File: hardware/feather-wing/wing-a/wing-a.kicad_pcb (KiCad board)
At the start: 2 copper layers, 50.8 x 22.9 mm, 29 parts, among them J1 USB-C plug, J2 Feather 16-pin, J3 Feather 12-pin, U2 AP22653W6-7, U3 USBLC6-2SC6, U4 USBLC6-2SC6

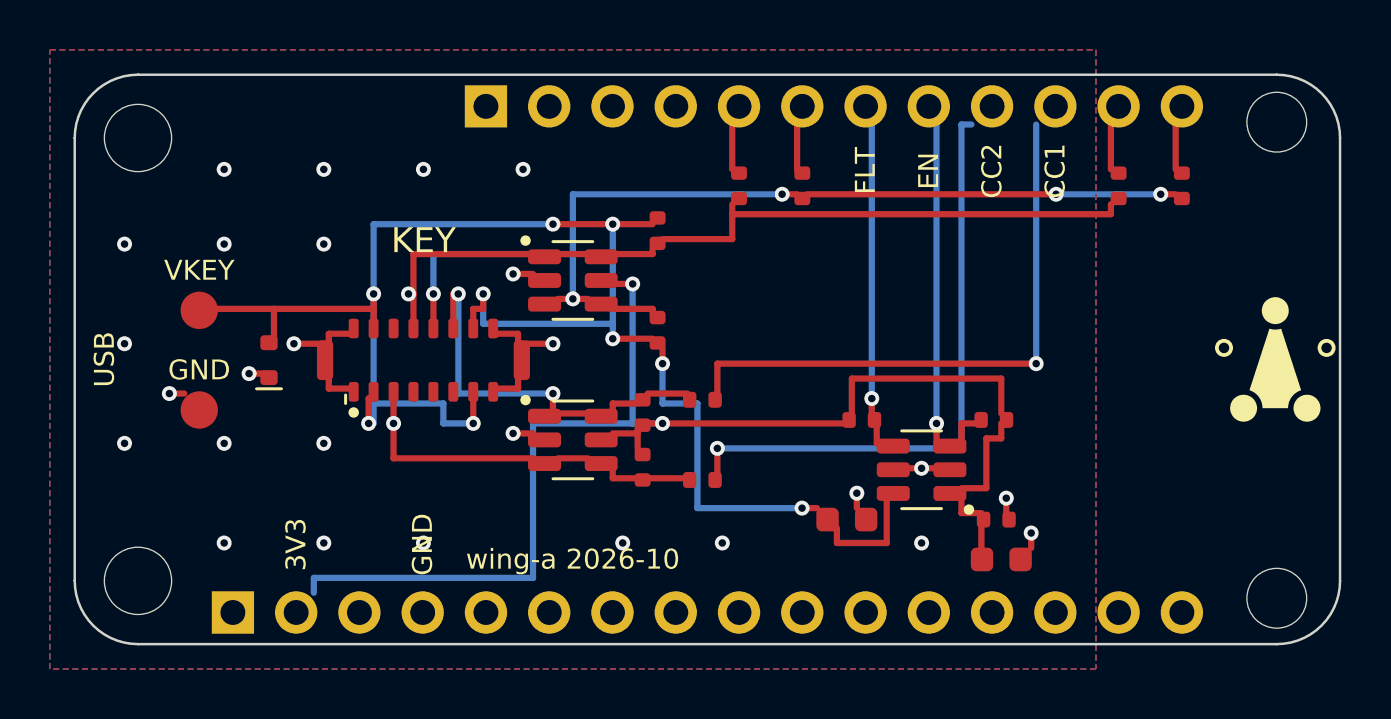
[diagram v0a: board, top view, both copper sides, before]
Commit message: wing-b: the key's plug at the edge, on a tab out of the 12-pin side
The same circuit as wing-a with GCT's USB4155 right-angle edge plug, so
key-c lies beside the stack. Every edge of the Feather's outline is taken,
so the plug sits on an 11 x 5 mm tab mid-board. The plug wants a 1.0 mm
board; only its A row can be routed, which is all key-c needs, so one CC
line is read (D5) and R4/R6 go. Its 0.5 mm pitch is fanned out on a 0.1 mm
grid with V-shaped stubs before the 0.2 mm router takes over.

The new courtyard check found five overlaps in wing-a as first pushed; those
parts moved, and both ESD arrays' flow-through pairs are now bridged under
the chip. Both wings self-check clean; neither has been through KiCad.

Co-Authored-By: Claude Opus 5.5 <noreply@anthropic.com>
Claude-Session: https://claude.ai/code/session_014UuUn7sLaEVq1c2M8i6TGa
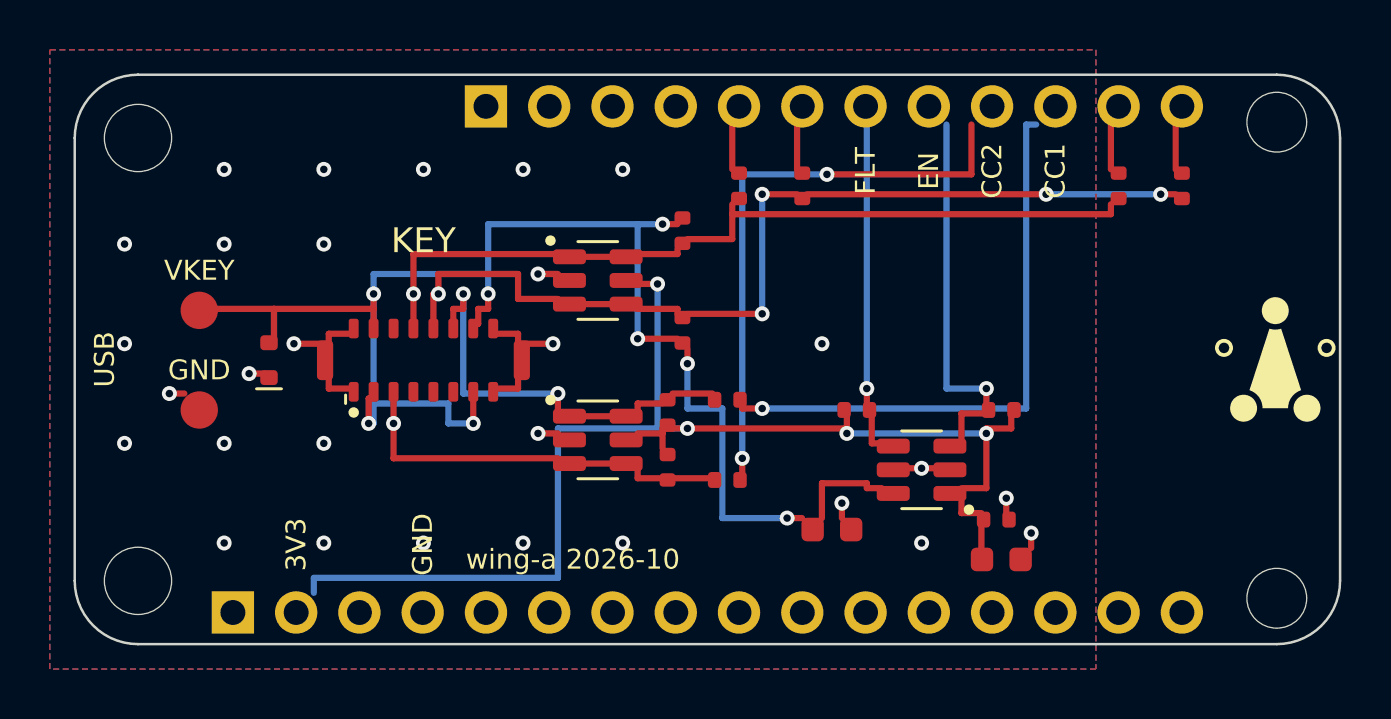
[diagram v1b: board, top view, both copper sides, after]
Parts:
- moved R1 1.00 mm to (124.4, 127.4)
- moved R2 1.00 mm to (124.4, 123.4)
- moved R3 1.00 mm to (123.8, 130.7)
- moved R4 1.00 mm to (123.8, 132.9)
- moved R5 1.00 mm to (126.2, 130.2)
- moved R6 1.00 mm to (126.2, 133.4)
- moved U3 1.00 mm to (121.0, 125.4)
- moved U4 1.00 mm to (121.0, 131.8)
- moved C2 0.72 mm to (130.4, 135.4)
- moved R7 0.50 mm to (137.2, 130.6)
- moved R8 0.45 mm to (131.4, 130.6)
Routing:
- net /VKEY: track 66.4 -> 60.4 mm, vias 9 -> 8
- net /KEY_SDA: track 39.4 -> 36.1 mm
- net /CC2: track 12.2 -> 14.3 mm
- net +3V3: track 52.4 -> 50.8 mm, vias 2 -> 4
- net /CC1: track 14.2 -> 15.5 mm
- net /CC2_SENSE: track 24.2 -> 23.2 mm, vias 1 -> 2
- net /KEY_SCL: track 30.6 -> 31.5 mm
- net /KEY_EN: track 14.2 -> 15.0 mm
- net GND: vias 27 -> 29

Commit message: wing-a and wing-b: KiCad-clean, key-c P3's LED line, wing-b on a straddle plug
KiCad 10.0.6 found what the self-check couldn't: gen_wing.py's rotate(),
shared with console-pocket, turned parts clockwise on the page where
KiCad turns them counter-clockwise, so every part at 90 or 270 had its
pads swapped against its tracks. rotate() is KiCad's now and ROT's 90s
and 270s are swapped; round pads join only inside their circle; loose
via and track ends are dropped. console-pocket's README now says not to
order it until it is regenerated the same way.

Both wings carry key-c P3's LED: A8 and B8 joined as KEY_LED, driven
from D13 (the status LED pin) through R13, D3 for ESD; R14 to A0 not
fitted. No firmware change.

wing-b is redrawn around a SHOU HAN 24P straddle-mount plug (C3151751)
on a tab out of the 12-pin side, in place of GCT's USB4155.

tools/keypcb fill then check, both wings: ERC 0, DRC 0, 0 unconnected,
parity clean. Fab files and renders in each wing's fab/. Not ordered.

Co-Authored-By: Claude Opus 5.5 <noreply@anthropic.com>
Claude-Session: https://claude.ai/code/session_014mGuGD4x9Si2dmdRKbhRec
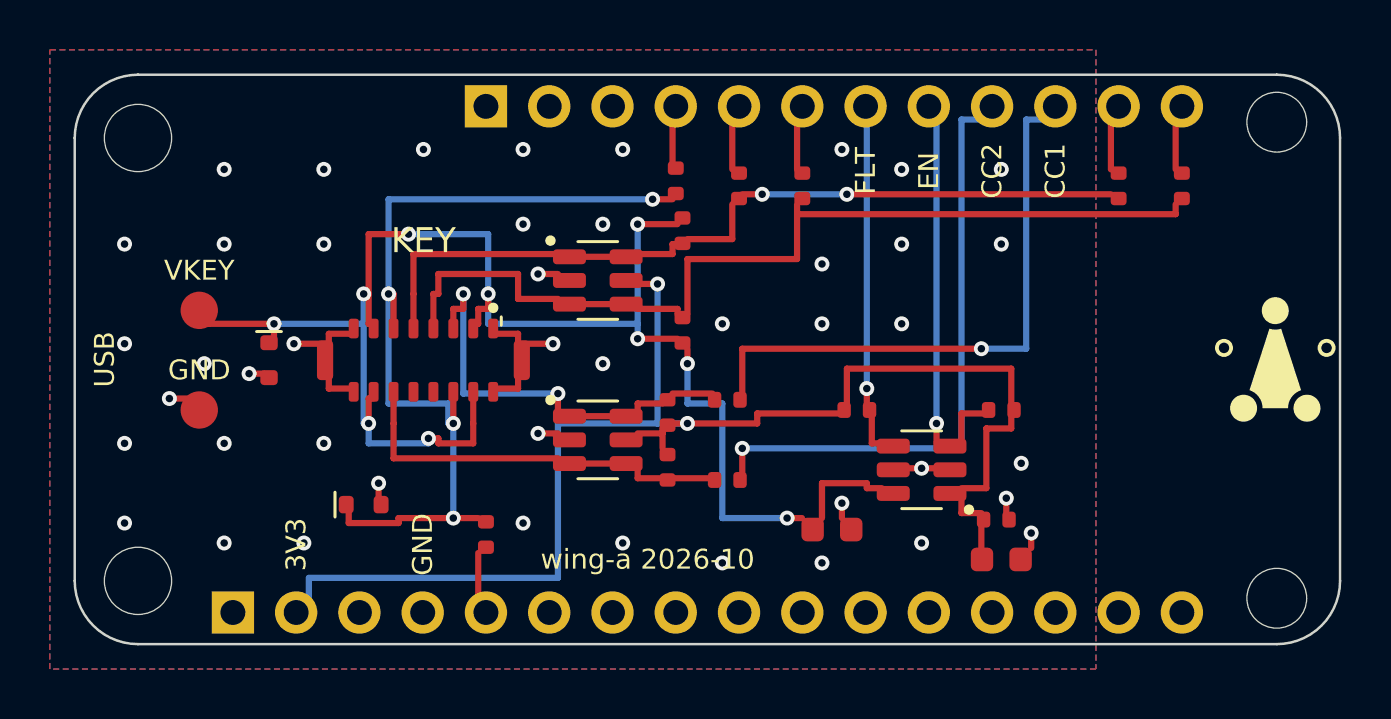
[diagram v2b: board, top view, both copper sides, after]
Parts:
- added D3: ESD5Z5V0, pqwing:D_SOD-523, F.Cu at (111.6, 134.4)
- added R13: 100, pqwing:R_0402, F.Cu at (124.1, 121.4)
- added R14: 100, pqwing:R_0402, F.Cu at (116.5, 135.6)
- turned D1 to -90 degrees
- turned J1 to -90 degrees
- turned R1 to 90 degrees
- turned R10 to 90 degrees
- turned R11 to 90 degrees
- turned R12 to 90 degrees
- turned R2 to -90 degrees
- turned R3 to 90 degrees
- turned R4 to -90 degrees
- turned R9 to 90 degrees
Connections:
- J1 pad A8: unconnected-(J1-SBU1-PadA8) -> /KEY_LED
- J1 pad B8: unconnected-(J1-SBU2-PadB8) -> /KEY_LED
- J2 pad 5: unconnected-(J2-A0-Pad5) -> /LED_ALT
- J3 pad 4: unconnected-(J3-D13-Pad4) -> /LED_D13
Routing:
- net /KEY_LED: track 0.00 -> 35.0 mm, vias 0 -> 4
- net /VKEY: track 60.4 -> 64.2 mm, vias 8 -> 10
- net +3V3: track 50.8 -> 54.4 mm, vias 4 -> 2
- net /LED_D13: track 0.00 -> 1.80 mm
- net /LED_ALT: track 0.00 -> 1.80 mm
- net GND: track 13.4 -> 14.2 mm, vias 29 -> 45
- net /CC2_SENSE: track 23.2 -> 23.8 mm, vias 2 -> 1
- net /KEY_SCL: track 31.5 -> 30.9 mm, vias 1 -> 2
- net /KEY_SDA: track 36.1 -> 36.5 mm, vias 5 -> 0
- net /CC2: vias 1 -> 0
